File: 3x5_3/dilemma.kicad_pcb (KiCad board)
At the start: 2 copper layers, 134.1 x 215.6 mm, 91 parts, among them J5001 BATTERY_CONN_DEANS, J5011 BATTERY_CONN_DEANS, SW101 NA_SW_Push, SW102 NA_SW_Push, SW103 NA_SW_Push, SW104 NA_SW_Push, SW105 NA_SW_Push, SW106 NA_SW_Push, SW107 NA_SW_Push, SW108 NA_SW_Push, SW109 NA_SW_Push, SW112 NA_SW_Push, SW113 NA_SW_Push, SW114 NA_SW_Push, SW115 NA_SW_Push, SW116 NA_SW_Push, SW117 NA_SW_Push, SW118 NA_SW_Push, SW119 NA_SW_Push, SW3001 NA_SW_Push, SW5002 NA_SW_Push, SW5003 NA_SW_Push, SW5004 NA_SW_Push, SW5005 NA_SW_Push, SW5006 NA_SW_Push, SW5007 NA_SW_Push, SW5008 NA_SW_Push, SW5009 NA_SW_Push, SW5010 NA_SW_Push, SW5011 NA_SW_Push, SW5012 NA_SW_Push, SW5013 NA_SW_Push, SW5014 NA_SW_Push, SW5015 NA_SW_Push, SW5016 NA_SW_Push, SW5017 NA_SW_Push, SW5018 NA_SW_Push, SW5019 NA_SW_Push, SW5021 SW_SPST, SW5022 SW_SPST, U5001 eliteC, U5007 eliteC

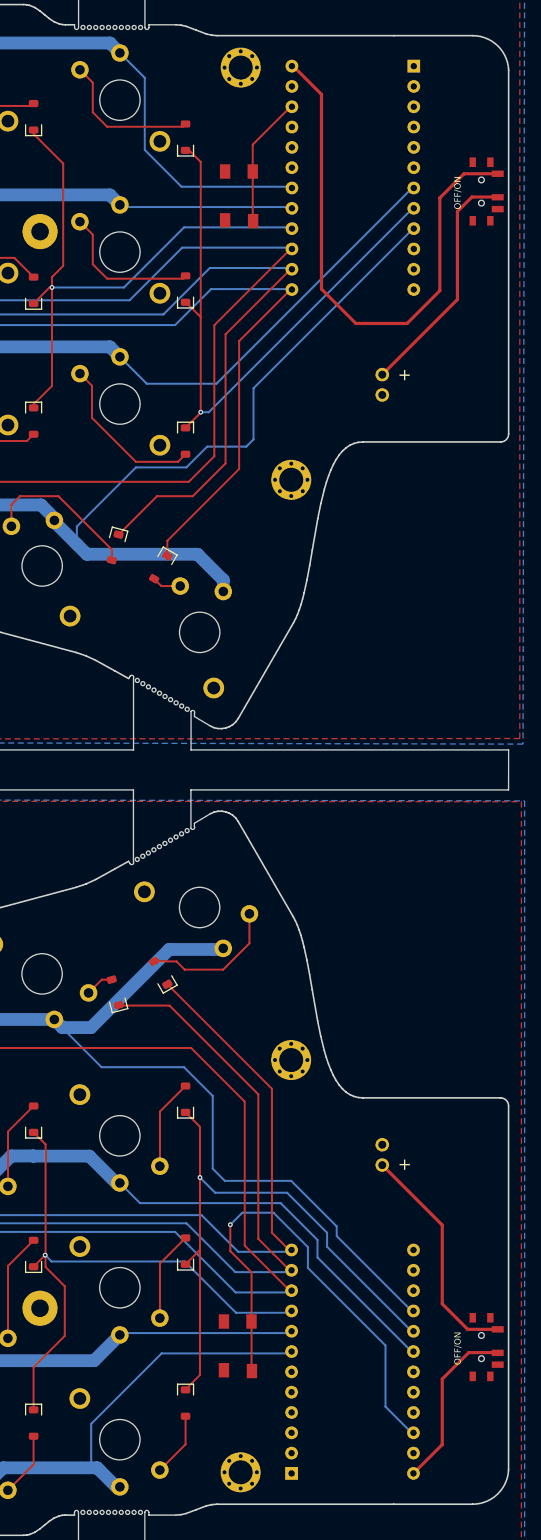
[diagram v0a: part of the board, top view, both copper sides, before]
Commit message: antenna cutout
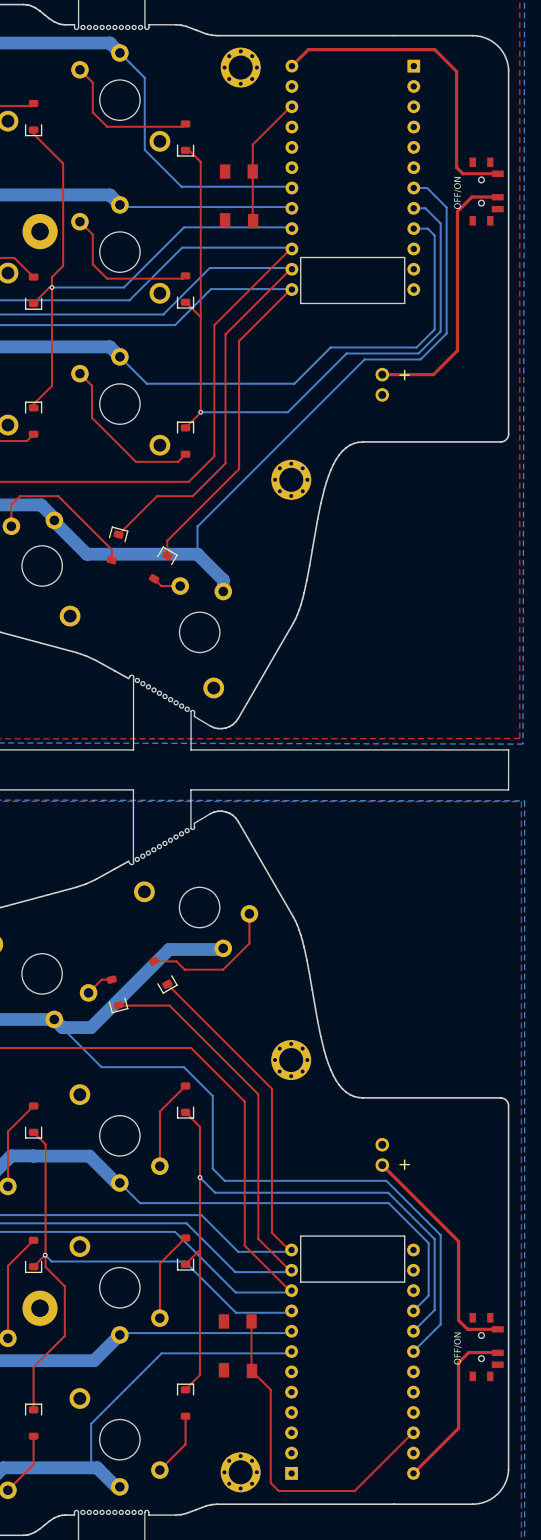
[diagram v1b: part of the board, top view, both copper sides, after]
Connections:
- U5001 pad 16: M_ROW1_L -> M_ROW4_L
- U5001 pad 18: M_ROW4_L -> M_ROW1_L
- U5007 pad 7: M_ROW4 -> M_ROW1
- U5007 pad 9: M_ROW1 -> M_ROW4
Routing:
- net BAT: track 67.9 -> 40.1 mm
- net RESET_L: track 60.4 -> 42.5 mm, vias 1 -> 0
- net M_ROW1_L: track 114.7 -> 129.3 mm
- net M_COL5: track 76.5 -> 91.0 mm
- net M_ROW4: track 137.9 -> 147.9 mm
- net M_COL5_L: track 74.9 -> 83.9 mm
- net M_ROW4_L: track 137.4 -> 141.5 mm
- net BAT_SW: track 30.1 -> 33.8 mm
- net M_ROW1: track 113.2 -> 115.2 mm
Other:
- outline, holes or cut-outs redrawn

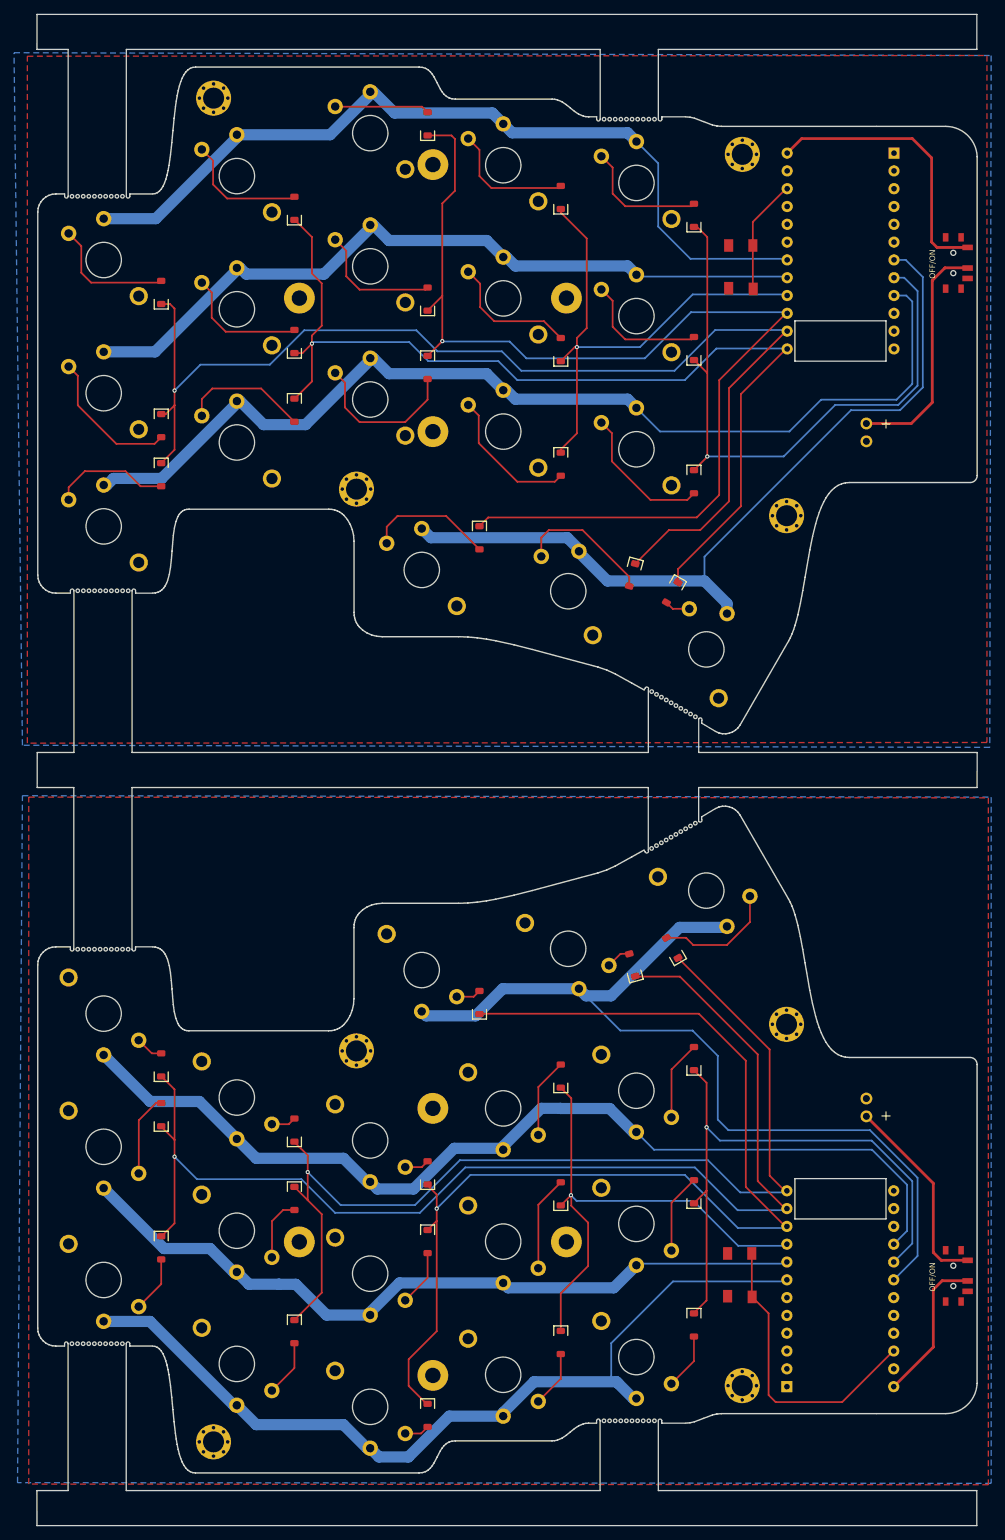
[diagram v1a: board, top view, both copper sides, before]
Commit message: convert to reversible pcb
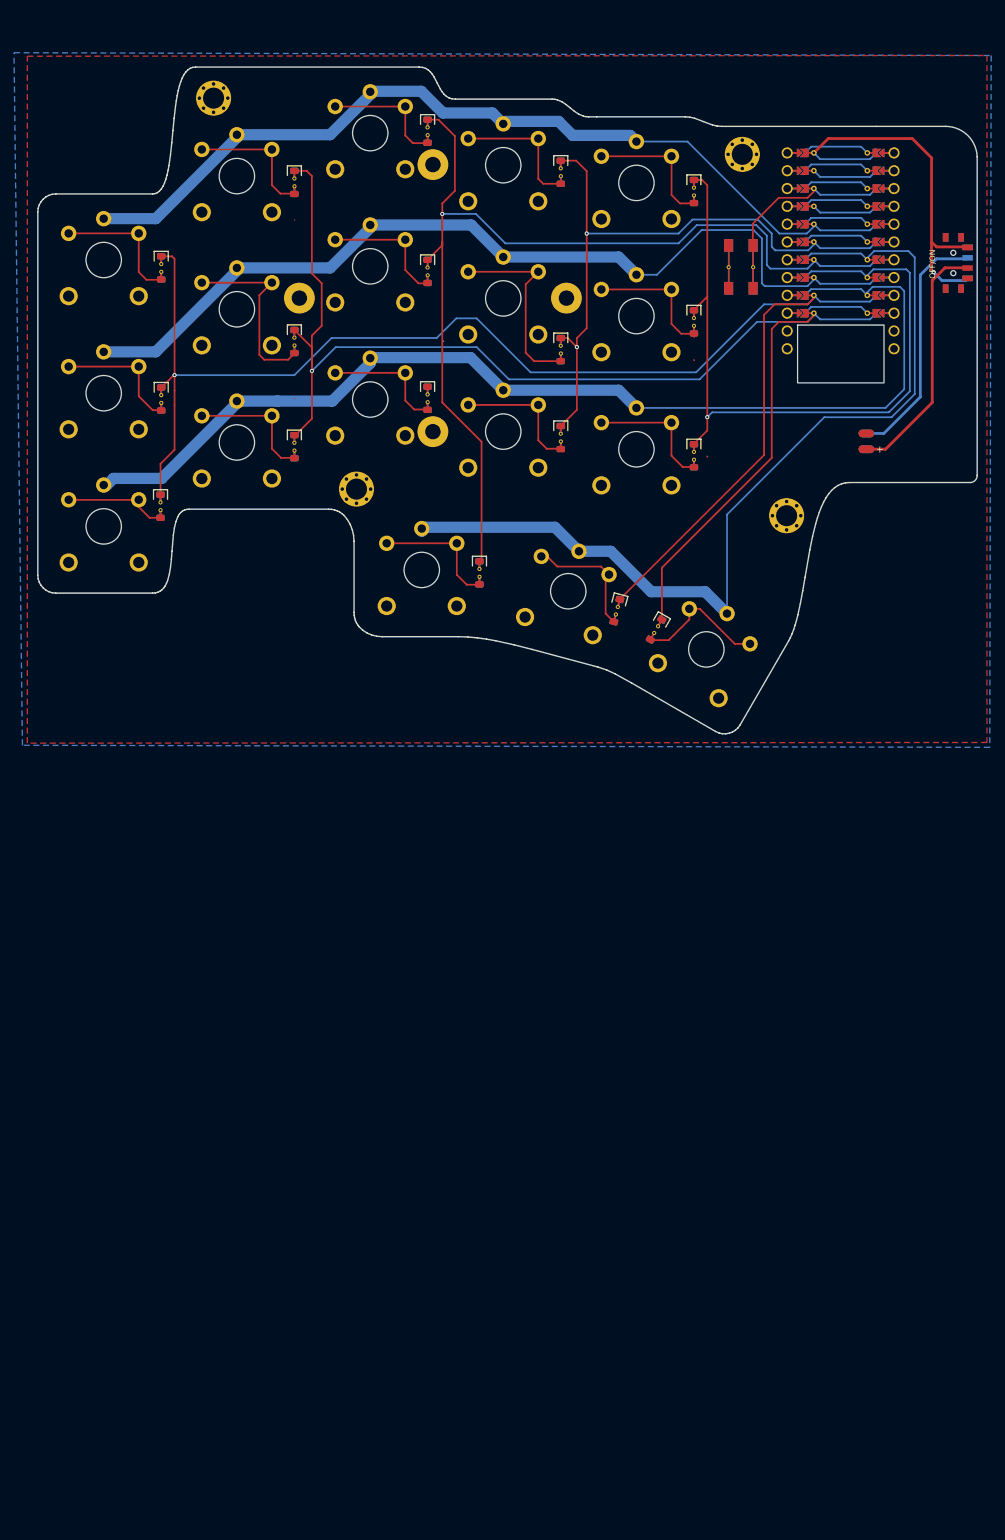
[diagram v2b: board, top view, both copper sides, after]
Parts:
- removed D5001, D5002, D5003, D5004, D5005, D5006, D5007, D5008, D5009, D5010, D5011, D5012, D5013, D5014, D5015, D5016, D5017, D5018: D, Diode_SMD:D_SOD-123
- removed H5001, H5002, H5003, H5007: NA_M4, local-libraries:MountingHole_3mm_Pad_Via
- removed H5008: NA_Mount, local-libraries:Tenting_Puck
- removed J5001: BATTERY_CONN_DEANS, local-libraries:battery_connector_THT
- removed PSW5002: SW_DPDT_x2, local-libraries:Switch_MSK-12C01-07
- removed SW5002, SW5003, SW5004, SW5005, SW5006, SW5007, SW5008, SW5009, SW5010, SW5011, SW5012, SW5013, SW5014, SW5015, SW5016, SW5017, SW5018, SW5019: NA_SW_Push, local-libraries:SW_Kailh_Choc_V2_1.00u
- removed SW5021: SW_SPST, Library:PushSwitch
- removed U5001: eliteC, local-libraries:Sparkfun_Pro_Micro
- D112, D115, D5031, D5032, D5033, D5034, D5035, D5036, D5037, D5038, D5039, D5040, D5041, D5042, D5043, D5044, D5045, D5046: footprint Diode_SMD:D_SOD-123 -> local-libraries:D_SOD-123_reversible
- J5011: footprint local-libraries:battery_connector_THT -> local-libraries:battery_pads_reversible
- PSW5001: footprint local-libraries:Switch_MSK-12C01-07 -> local-libraries:Switch_MSK-12C01-07_reversible
- SW101, SW102, SW103, SW104, SW105, SW106, SW107, SW108, SW109, SW112, SW113, SW114, SW115, SW116, SW117, SW118, SW119, SW3001: footprint local-libraries:SW_Kailh_Choc_V2_1.00u -> local-libraries:SW_Kailh_Choc_V2_1.00u_reversible
- SW5022: footprint Library:PushSwitch -> local-libraries:reset_switch_reversible
- U5007: footprint local-libraries:Sparkfun_Pro_Micro -> local-libraries:nice!nano_reversible; moved to F.Cu
- moved U5007 17.1 mm to (227.0, 51.1)
- moved D5038 5.78 mm to (200.7, 106.5)
- moved D5034 5.55 mm to (195.1, 103.8)
- moved D5037 5.20 mm to (149.1, 80.4)
- moved D5042 5.00 mm to (175.5, 98.4)
- moved D5033 4.50 mm to (130.0, 88.9)
- moved D5041 4.40 mm to (168.1, 73.5)
- moved D5040 3.95 mm to (168.1, 55.4), turned to -90 degrees
- moved D5046 3.80 mm to (206.1, 62.6), turned to -90 degrees
- moved D112 3.80 mm to (187.1, 79.1)
- moved D5032 3.80 mm to (130.1, 73.6)
- moved D115 3.70 mm to (206.1, 81.7)
- moved D5035 3.70 mm to (149.1, 42.7), turned to -90 degrees
- moved D5043 3.60 mm to (187.1, 41.2), turned to -90 degrees
- moved D5031 3.50 mm to (130.1, 54.9), turned to -90 degrees
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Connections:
- U5007 pad 15: M_COL3 -> M_COL2
- U5007 pad 16: M_COL4 -> M_COL1
- U5007 pad 18: M_ROW2 -> M_COL3
- U5007 pad 19: unconnected-(U5007-F5-Pad19) -> M_COL4
- U5007 pad 20: unconnected-(U5007-F4-Pad20) -> M_ROW2
- U5007 pad 21: VCC -> unconnected-(U5007-VCC-Pad21)
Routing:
- net M_COL1_L: track 169.1 -> 0.00 mm, vias 1 -> 0
- net M_COL3_L: track 158.7 -> 0.00 mm, vias 1 -> 0
- net M_COL2_L: track 146.2 -> 0.00 mm, vias 1 -> 0
- net M_ROW4_L: track 141.5 -> 0.00 mm
- net M_ROW1_L: track 129.3 -> 0.00 mm
- net M_ROW2_L: track 124.6 -> 0.00 mm
- net M_ROW3_L: track 108.8 -> 0.00 mm
- net M_COL5_L: track 83.9 -> 0.00 mm, vias 1 -> 0
- net M_COL4_L: track 73.9 -> 0.00 mm, vias 1 -> 0
- net RESET_L: track 42.5 -> 0.00 mm
- net M_COL2: track 143.8 -> 183.1 mm
- net BAT_SW: track 33.8 -> 70.4 mm
- net M_COL1: track 168.1 -> 199.3 mm
- net BAT_SW_L: track 28.8 -> 0.00 mm
- net M_COL3: track 159.6 -> 133.9 mm
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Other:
- board size 134.1 x 215.6 mm -> 134 x 95.1 mm

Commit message: refill zones
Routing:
- net BAT_SW: track 70.4 -> 71.8 mm
- net M_COL4: vias 2 -> 1
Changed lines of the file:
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@@
-	)
-	(segment
-		(start 131.968798 80.821819)
-		(end 131.968798 74.471819)
-		(width 0.25)
-		(layer "F.Cu")
-		(net 1)
-	)
-	(segment
-		(start 131.968798 72.371819)
-		(end 131.968798 74.471819)
-		(width 0.25)
-		(layer "F.Cu")
-		(net 1)
 	)
 	(segment
@@
 	(segment
 		(start 131.968798 70.171819)
-		(end 131.968798 72.371819)
+		(end 131.968798 80.821819)
 		(width 0.25)
 		(layer "F.Cu")
@@
 		(end 150.818798 41.021819)
 		(width 0.25)
-		(layer "F.Cu")
-		(net 2)
-	)
-	(segment
-		(start 149.068798 73.521819)
-		(end 149.118798 73.521819)
-		(width 0.16)
 		(layer "F.Cu")
 		(net 2)
@@
 	)
 	(segment
-		(start 170.168798 65.321819)
-		(end 170.318798 65.321819)
-		(width 0.16)
-		(layer "B.Cu")
-		(net 3)
-	)
-	(segment
 		(start 179.168798 51.371819)
 		(end 203.868798 51.371819)
@@
 		(end 214.968798 48.771819)
 		(width 0.25)
-		(layer "B.Cu")
-		(net 3)
-	)
-	(segment
-		(start 170.318798 65.321819)
-		(end 170.368798 65.371819)
-		(width 0.16)
 		(layer "B.Cu")
 		(net 3)
@@
 		(net 4)
 	)
-	(via
-		(at 189.368798 66.171819)
-		(size 0.6)
-		(drill 0.3)
-		(layers "F.Cu" "B.Cu")
-		(teardrops
-			(best_length_ratio 0.5)
-			(max_length 1)
-			(best_width_ratio 1)
-			(max_width 2)
-			(curve_points 5)
-			(filter_ratio 0.9)
-			(enabled yes)
-			(allow_two_segments yes)
-			(prefer_zone_connections yes)
-		)
-		(net 4)
-	)
 	(segment
 		(start 222.368798 52.371819)
@@
 	)
 	(segment
+		(start 159.888808 68.451809)
+		(end 159.888808 67.7475)
+		(width 1.6)
+		(layer "B.Cu")
+		(net 8)
+	)
+	(segment
+		(start 197.863808 74.8475)
+		(end 233.393117 74.8475)
+		(width 0.25)
+		(layer "B.Cu")
+		(net 8)
+	)
+	(segment
+		(start 122.313808 85.8475)
+		(end 123.889489 84.271819)
+		(width 1.6)
+		(layer "B.Cu")
+		(net 8)
+	)
+	(segment
+		(start 140.863808 74.176809)
+		(end 140.863808 73.8725)
+		(width 1.6)
+		(layer "B.Cu")
+		(net 8)
+	)
+	(segment
+		(start 160.308818 67.671819)
+		(end 174.213127 67.671819)
+		(width 1.6)
+		(layer "B.Cu")
+		(net 8)
+	)
+	(segment
+		(start 146.668798 73.871819)
+		(end 154.468798 73.871819)
+		(width 1.6)
+		(layer "B.Cu")
+		(net 8)
+	)
+	(segment
+		(start 130.768798 84.271819)
+		(end 140.863808 74.176809)
+		(width 1.6)
+		(layer "B.Cu")
+		(net 8)
+	)
+	(segment
+		(start 236.068798 72.171819)
+		(end 236.068798 58.171819)
+		(width 0.25)
+		(layer "B.Cu")
+		(net 8)
+	)
+	(segment
+		(start 123.889489 84.271819)
+		(end 130.768798 84.271819)
+		(width 1.6)
+		(layer "B.Cu")
+		(net 8)
+	)
+	(segment
 		(start 121.863808 85.8475)
 		(end 122.313808 85.8475)
@@
 	)
 	(segment
-		(start 159.888808 68.451809)
-		(end 159.888808 67.7475)
-		(width 1.6)
-		(layer "B.Cu")
-		(net 8)
-	)
-	(segment
-		(start 197.863808 74.8475)
-		(end 233.393117 74.8475)
-		(width 0.25)
-		(layer "B.Cu")
-		(net 8)
-	)
-	(segment
-		(start 130.130617 84.91)
-		(end 140.863808 74.176809)
-		(width 1.6)
-		(layer "B.Cu")
-		(net 8)
-	)
-	(segment
-		(start 160.308818 67.671819)
-		(end 174.213127 67.671819)
-		(width 1.6)
-		(layer "B.Cu")
-		(net 8)
-	)
-	(segment
-		(start 146.668798 73.871819)
-		(end 154.468798 73.871819)
-		(width 1.6)
-		(layer "B.Cu")
-		(net 8)
-	)
-	(segment
-		(start 236.068798 72.171819)
-		(end 236.068798 58.171819)
-		(width 0.25)
-		(layer "B.Cu")
-		(net 8)
-	)
-	(segment
-		(start 129.96625 84.904942)
-		(end 129.971308 84.91)
-		(width 1.6)
-		(layer "B.Cu")
-		(net 8)
-	)
-	(segment
 		(start 233.393117 74.8475)
 		(end 236.068798 72.171819)
@@
 	)
 	(segment
-		(start 122.313808 85.8475)
-		(end 123.256366 84.904942)
-		(width 1.6)
-		(layer "B.Cu")
-		(net 8)
-	)
-	(segment
 		(start 159.888808 68.091829)
 		(end 160.308818 67.671819)
@@
 	)
 	(segment
-		(start 123.256366 84.904942)
-		(end 129.96625 84.904942)
-		(width 1.6)
-		(layer "B.Cu")
-		(net 8)
-	)
-	(segment
 		(start 178.863808 72.3225)
 		(end 195.338808 72.3225)
@@
 	)
 	(segment
-		(start 129.971308 84.91)
-		(end 130.130617 84.91)
-		(width 1.6)
-		(layer "B.Cu")
-		(net 8)
-	)
-	(segment
 		(start 140.863808 73.8725)
 		(end 146.668117 73.8725)
@@
 	)
 	(segment
-		(start 140.863808 74.176809)
-		(end 140.863808 73.8725)
-		(width 1.6)
-		(layer "B.Cu")
-		(net 8)
-	)
-	(segment
 		(start 159.888808 67.7475)
 		(end 159.888808 68.091829)
@@
 	)
 	(segment
-		(start 149.068798 48.021819)
-		(end 149.118798 48.021819)
-		(width 0.16)
-		(layer "F.Cu")
-		(net 14)
-	)
-	(segment
 		(start 148.168798 67.971819)
 		(end 144.768798 67.971819)
@@
 	)
 	(segment
-		(start 154.888808 31.8475)
-		(end 154.913127 31.871819)
-		(width 0.25)
-		(layer "F.Cu")
-		(net 18)
-	)
-	(segment
 		(start 168.018798 37.071819)
 		(end 168.068798 37.021819)
@@
 	)
 	(segment
-		(start 206.068798 64.721819)
-		(end 206.068798 64.671819)
-		(width 0.25)
-		(layer "F.Cu")
-		(net 27)
-	)
-	(segment
 		(start 206.018798 64.271819)
 		(end 206.068798 64.221819)
@@
 		(start 192.863808 57.9475)
 		(end 202.863808 57.9475)
-		(width 0.25)
-		(layer "F.Cu")
-		(net 27)
-	)
-	(segment
-		(start 206.068798 68.021819)
-		(end 206.118798 68.021819)
 		(width 0.25)
 		(layer "F.Cu")
@@
 	)
 	(segment
+		(start 240.668798 53.571819)
+		(end 244.968798 53.571819)
+		(width 0.4)
+		(layer "B.Cu")
+		(net 29)
+	)
+	(segment
+		(start 235.653798 78.486819)
+		(end 240.068798 74.071819)
+		(width 0.4)
+		(layer "B.Cu")
+		(net 29)
+	)
+	(segment
+		(start 230.668798 78.486819)
+		(end 235.653798 78.486819)
+		(width 0.4)
+		(layer "B.Cu")
+		(net 29)
+	)
+	(segment
 		(start 244.968798 53.571819)
 		(end 245.108798 53.431819)
@@
 	)
 	(segment
-		(start 233.153798 78.486819)
-		(end 238.368798 73.271819)
+		(start 240.068798 74.071819)
+		(end 240.068798 54.171819)
 		(width 0.4)
 		(layer "B.Cu")
@@
 	)
 	(segment
-		(start 230.668798 78.486819)
-		(end 233.153798 78.486819)
-		(width 0.4)
-		(layer "B.Cu")
-		(net 29)
-	)
-	(segment
-		(start 238.368798 73.271819)
-		(end 238.368798 55.871819)
-		(width 0.4)
-		(layer "B.Cu")
-		(net 29)
-	)
-	(segment
-		(start 240.668798 53.571819)
-		(end 244.968798 53.571819)
-		(width 0.4)
-		(layer "B.Cu")
-		(net 29)
-	)
-	(segment
-		(start 238.368798 55.871819)
+		(start 240.068798 54.171819)
 		(end 240.668798 53.571819)
 		(width 0.4)
